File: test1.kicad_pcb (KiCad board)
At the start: 2 copper layers, 45.7 x 91.4 mm, 22 parts, among them P1 Conn_01x03, P2 Conn_01x02, P3 Conn_01x04, U1 L78L05_TO92, U2 LM339

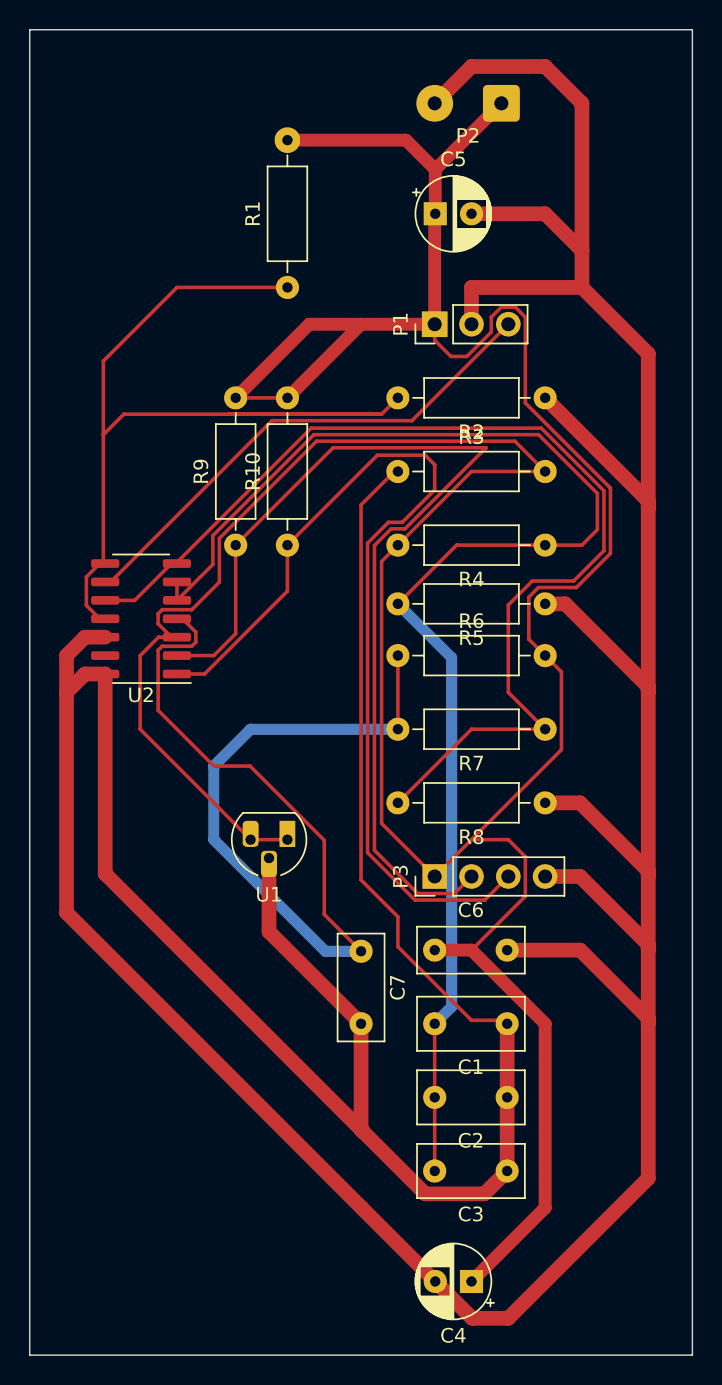
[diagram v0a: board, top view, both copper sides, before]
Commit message: updated wire sizes
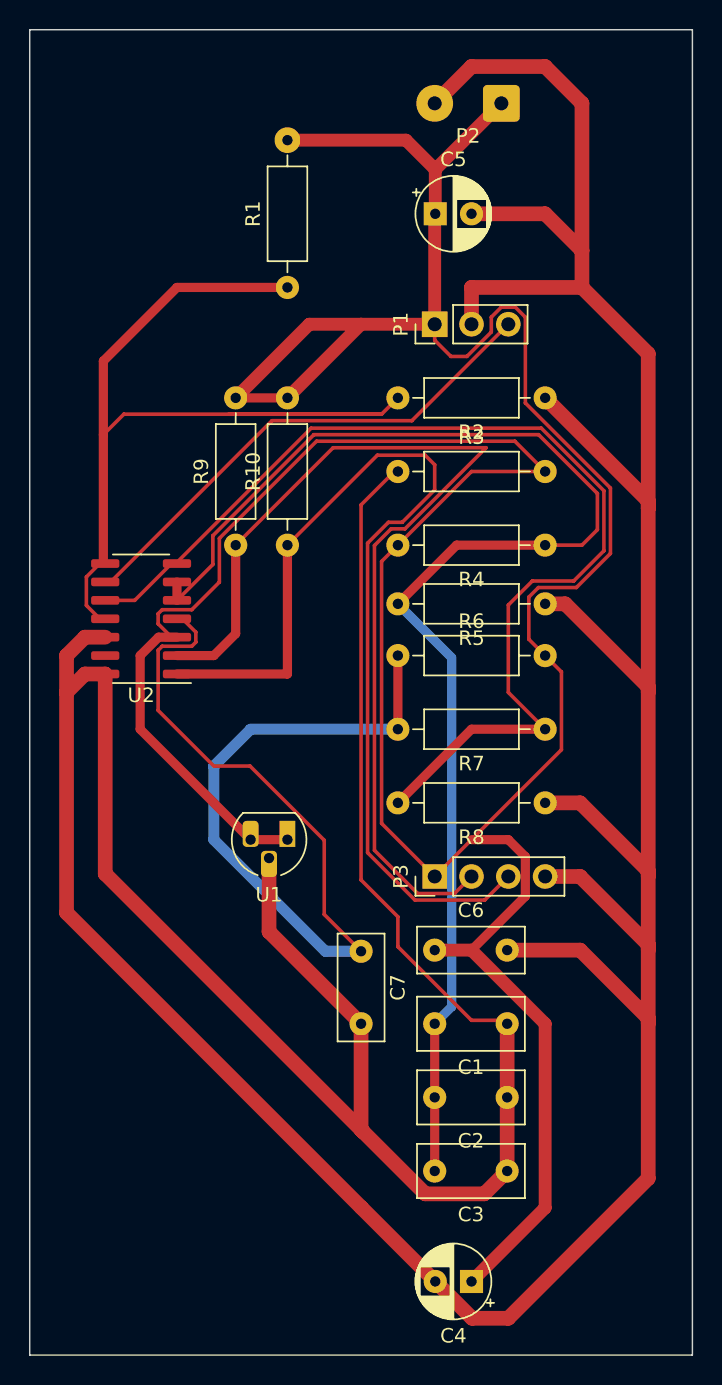
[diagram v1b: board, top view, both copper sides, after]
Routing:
- net Net-(P3-Pin_3): track 67.1 -> 70.5 mm
